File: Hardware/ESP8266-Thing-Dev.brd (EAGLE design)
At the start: 55.2 x 25.4 mm, 70 parts, among them J1 DNP, Q1 MMBT2222A, Q2 MMBT2222A, U1 AP2112K-3.3V, U2 ESP8266, U3 AT25SF041-SOIC8, U4 FTS31XS-U, Y1 26MHz

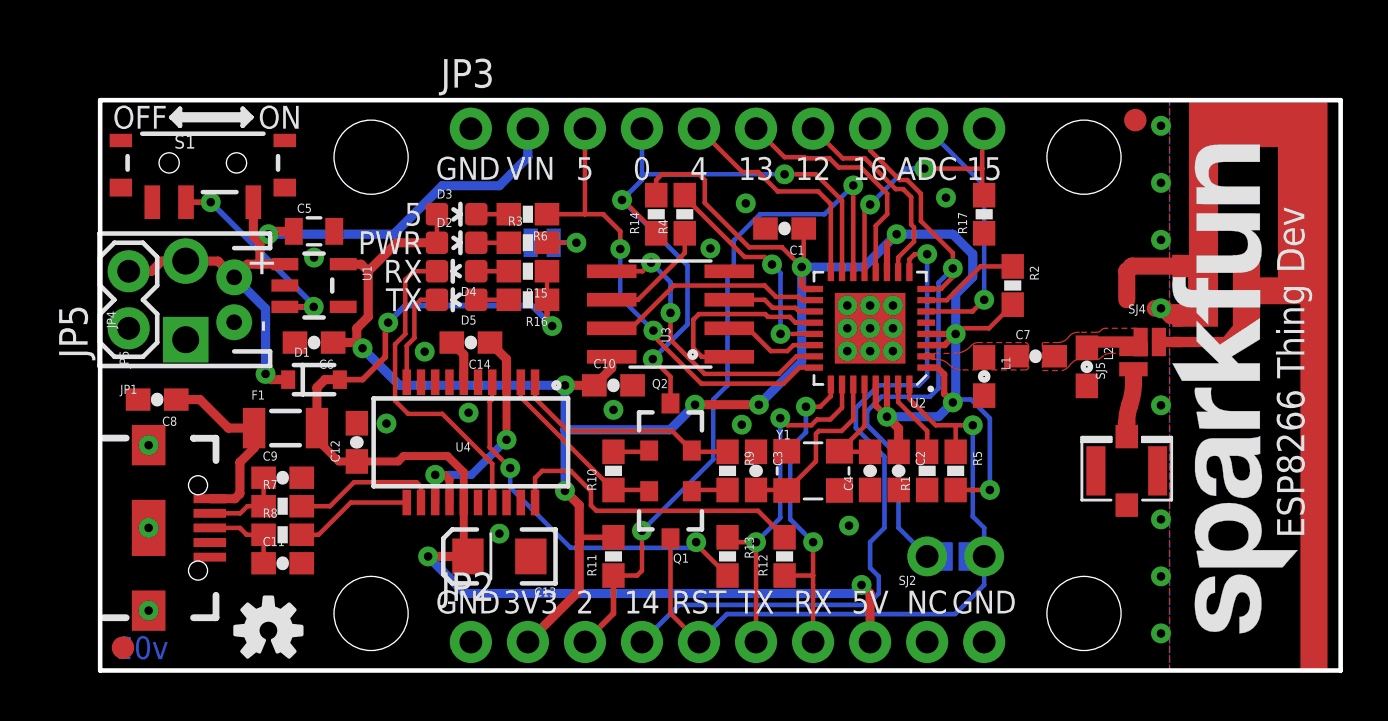
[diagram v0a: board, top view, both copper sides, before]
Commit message: Extending dimensions borders past antenna copper.
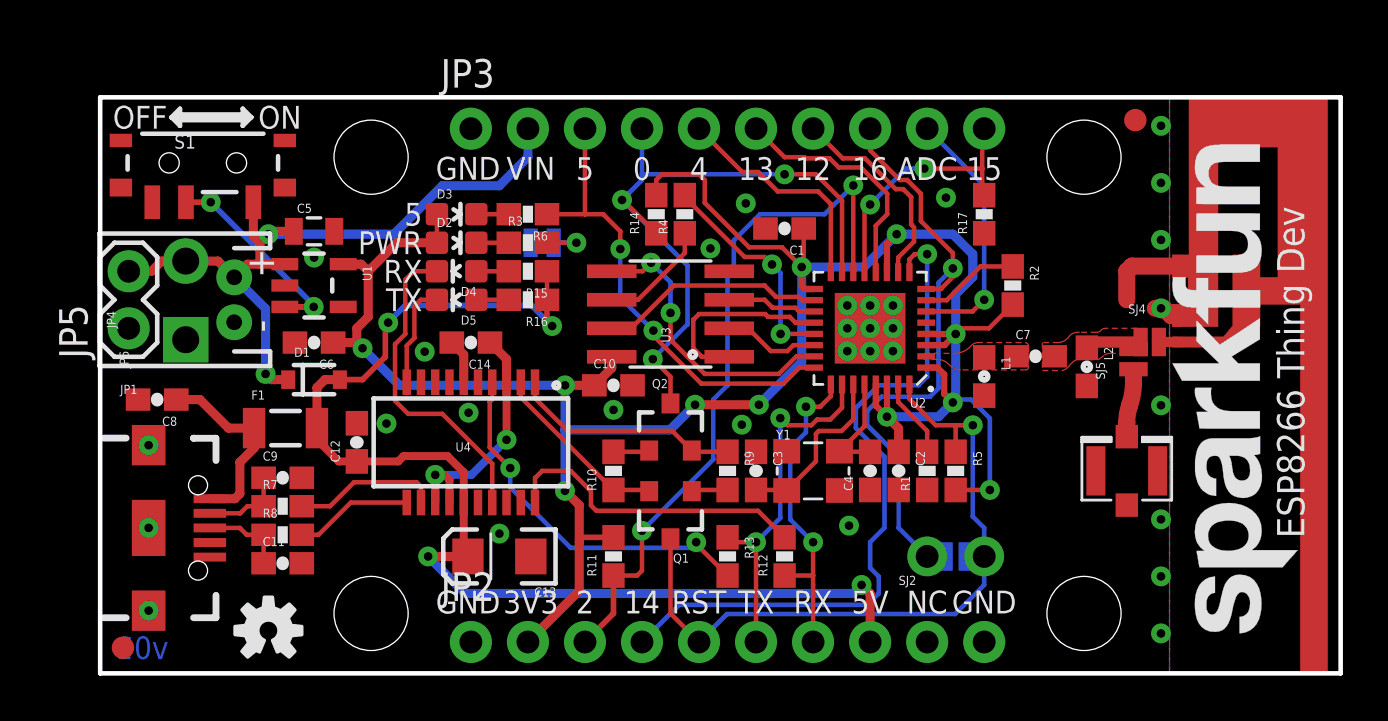
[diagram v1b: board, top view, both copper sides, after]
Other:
- board size 55.2 x 25.4 mm -> 55.2 x 25.7 mm
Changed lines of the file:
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@@
 <layer number="47" name="Measures" color="7" fill="1" visible="no" active="yes"/>
 <layer number="48" name="Document" color="7" fill="1" visible="no" active="yes"/>
-<layer number="49" name="Reference" color="7" fill="1" visible="yes" active="yes"/>
+<layer number="49" name="Reference" color="7" fill="1" visible="no" active="yes"/>
 <layer number="50" name="dxf" color="7" fill="1" visible="no" active="no"/>
 <layer number="51" name="tDocu" color="6" fill="1" visible="yes" active="yes"/>
@@
 <board>
 <plain>
-<wire x1="0" y1="0" x2="0" y2="25.4" width="0.2032" layer="20"/>
-<wire x1="0" y1="25.4" x2="55.245" y2="25.4" width="0.2032" layer="20"/>
-<wire x1="55.245" y1="25.4" x2="55.245" y2="0" width="0.2032" layer="20"/>
-<wire x1="55.245" y1="0" x2="0" y2="0" width="0.2032" layer="20"/>
+<wire x1="0" y1="-0.127" x2="0" y2="25.527" width="0.2032" layer="20"/>
+<wire x1="0" y1="25.527" x2="55.245" y2="25.527" width="0.2032" layer="20"/>
+<wire x1="55.245" y1="25.527" x2="55.245" y2="-0.127" width="0.2032" layer="20"/>
+<wire x1="55.245" y1="-0.127" x2="0" y2="-0.127" width="0.2032" layer="20"/>
 <text x="1.778" y="24.638" size="1.016" layer="21" font="vector" ratio="15" align="center">OFF</text>
 <text x="8.001" y="24.638" size="1.016" layer="21" font="vector" ratio="15" align="center">ON</text>
@@
 <contactref element="S1" pad="1"/>
 <polygon width="0.254" layer="16" isolate="0.3048" rank="6">
-<vertex x="0" y="0"/>
-<vertex x="0" y="25.4"/>
-<vertex x="47.625" y="25.4"/>
-<vertex x="47.625" y="0"/>
+<vertex x="0" y="-0.127"/>
+<vertex x="0" y="25.527"/>
+<vertex x="47.625" y="25.527"/>
+<vertex x="47.625" y="-0.127"/>
 </polygon>
 <polygon width="0.254" layer="1" isolate="0.3048" rank="6">
-<vertex x="0" y="25.4"/>
-<vertex x="0" y="0"/>
-<vertex x="47.625" y="0"/>
-<vertex x="47.625" y="25.4"/>
+<vertex x="0" y="25.527"/>
+<vertex x="0" y="-0.127"/>
+<vertex x="47.625" y="-0.127"/>
+<vertex x="47.625" y="25.527"/>
 </polygon>
 <via x="34.29" y="15.24" extent="1-16" drill="0.381"/>

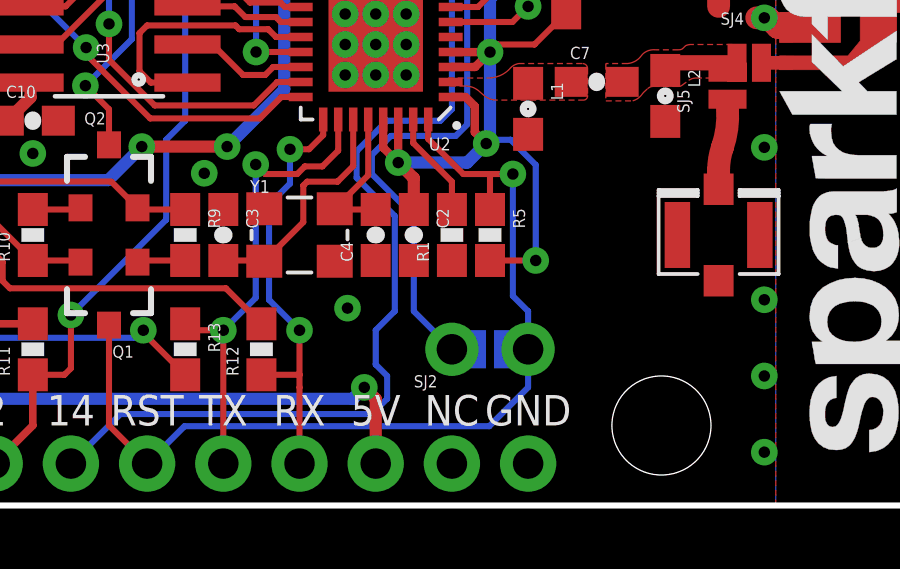
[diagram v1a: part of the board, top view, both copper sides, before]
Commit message: Removing SJ3 - SMD sleep jumper
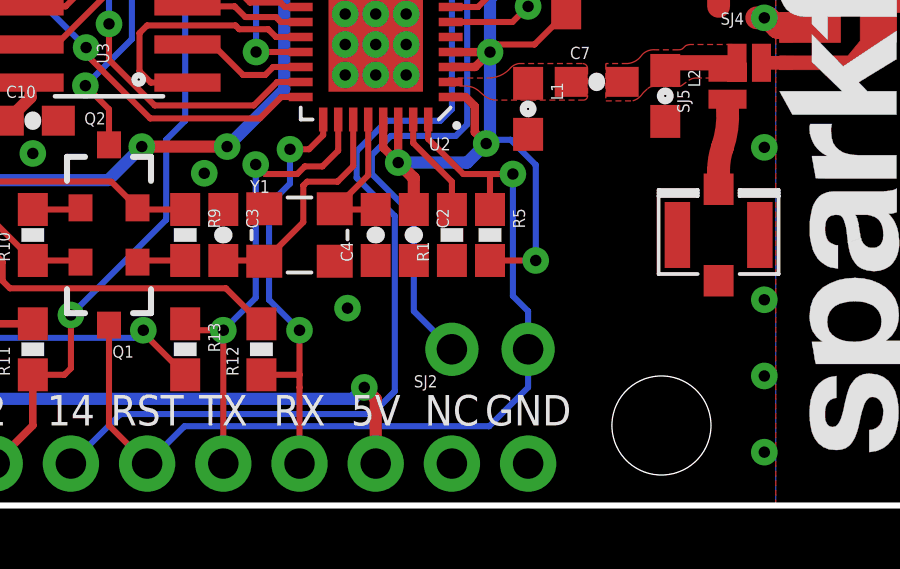
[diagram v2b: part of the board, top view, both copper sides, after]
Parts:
- removed SJ3: SLEEP-SMD, SparkFun-Passives:PAD-JUMPER-2-NO_NO_SILK
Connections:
- net GPIO16: no longer SJ3.1
- net RESET: no longer SJ3.2
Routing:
- net RESET: track 32.2 -> 31.4 mm
- net GPIO16: track 27.3 -> 26.5 mm
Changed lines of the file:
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@@
 <setting verticaltext="up"/>
 </settings>
-<grid distance="0.05" unitdist="inch" unit="inch" style="lines" multiple="1" display="yes" altdistance="0.005" altunitdist="inch" altunit="inch"/>
+<grid distance="0.05" unitdist="inch" unit="inch" style="lines" multiple="1" display="yes" altdistance="0.0025" altunitdist="inch" altunit="inch"/>
 <layers>
 <layer number="1" name="Top" color="4" fill="1" visible="yes" active="yes"/>
@@
 <attribute name="PROD_ID" value="RES-00824" x="22.86" y="8.89" size="1.778" layer="27" font="vector" ratio="15" rot="R90" display="off"/>
 </element>
-<element name="SJ3" library="SparkFun-Passives" package="PAD-JUMPER-2-NO_NO_SILK" value="SLEEP-SMD" x="38.1" y="5.08" rot="MR180"/>
 <element name="FID2" library="SparkFun-Aesthetics" package="FIDUCIAL-1X2" value="FIDUCIAL1X2" x="1.016" y="1.016"/>
 <element name="FID1" library="SparkFun-Aesthetics" package="FIDUCIAL-1X2" value="FIDUCIAL1X2" x="46.101" y="24.511"/>
@@
 <wire x1="38.1" y1="10.922" x2="38.862" y2="10.922" width="0.2032" layer="1"/>
 <wire x1="38.1" y1="9.74" x2="38.1" y2="10.922" width="0.2032" layer="1"/>
-<contactref element="SJ3" pad="2"/>
 <wire x1="38.862" y1="6.858" x2="39.37" y2="6.35" width="0.2032" layer="16"/>
 <wire x1="39.37" y1="6.35" x2="39.37" y2="5.08" width="0.2032" layer="16"/>
 <wire x1="38.0746" y1="2.5146" x2="39.37" y2="3.81" width="0.2032" layer="16"/>
 <wire x1="39.37" y1="3.81" x2="39.37" y2="5.08" width="0.2032" layer="16"/>
-<wire x1="38.55" y1="5.08" x2="39.37" y2="5.08" width="0.2032" layer="16"/>
 </signal>
 <signal name="LNA">
@@
 <wire x1="36.449" y1="12.7" x2="34.671" y2="12.7" width="0.2032" layer="16"/>
 <wire x1="34.671" y1="12.7" x2="33.655" y2="11.684" width="0.2032" layer="16"/>
-<wire x1="34.163" y1="2.921" x2="34.671" y2="3.429" width="0.2032" layer="16"/>
+<wire x1="34.163" y1="2.921" x2="34.925" y2="3.683" width="0.2032" layer="16"/>
 <wire x1="34.163" y1="2.921" x2="25.781" y2="2.921" width="0.2032" layer="16"/>
 <wire x1="25.781" y1="2.921" x2="24.13" y2="1.27" width="0.2032" layer="16"/>
-<wire x1="34.671" y1="3.429" x2="34.671" y2="4.191" width="0.2032" layer="16"/>
-<wire x1="34.671" y1="4.191" x2="34.29" y2="4.572" width="0.2032" layer="16"/>
-<wire x1="34.29" y1="4.572" x2="34.29" y2="5.715" width="0.2032" layer="16"/>
-<wire x1="34.29" y1="5.715" x2="34.925" y2="6.35" width="0.2032" layer="16"/>
-<wire x1="34.925" y1="6.35" x2="34.925" y2="9.525" width="0.2032" layer="16"/>
+<wire x1="34.925" y1="3.683" x2="34.925" y2="9.525" width="0.2032" layer="16"/>
 <wire x1="34.925" y1="9.525" x2="33.655" y2="10.795" width="0.2032" layer="16"/>
 <wire x1="33.655" y1="10.795" x2="33.655" y2="11.684" width="0.2032" layer="16"/>
@@
 <wire x1="35.56" y1="6.35" x2="36.83" y2="5.08" width="0.2032" layer="16"/>
 <contactref element="U2" pad="8"/>
-<contactref element="SJ3" pad="1"/>
-<wire x1="37.65" y1="5.08" x2="36.83" y2="5.08" width="0.2032" layer="16"/>
 <wire x1="36.79" y1="16.99" x2="37.437" y2="16.99" width="0.2032" layer="1"/>
 <wire x1="37.437" y1="16.99" x2="37.465" y2="17.018" width="0.2032" layer="1"/>

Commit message: Adjusting label header silk a bit
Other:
- board text added: "v10"
- board text removed: "v01"
